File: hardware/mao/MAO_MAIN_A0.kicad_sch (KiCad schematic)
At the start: 0 parts

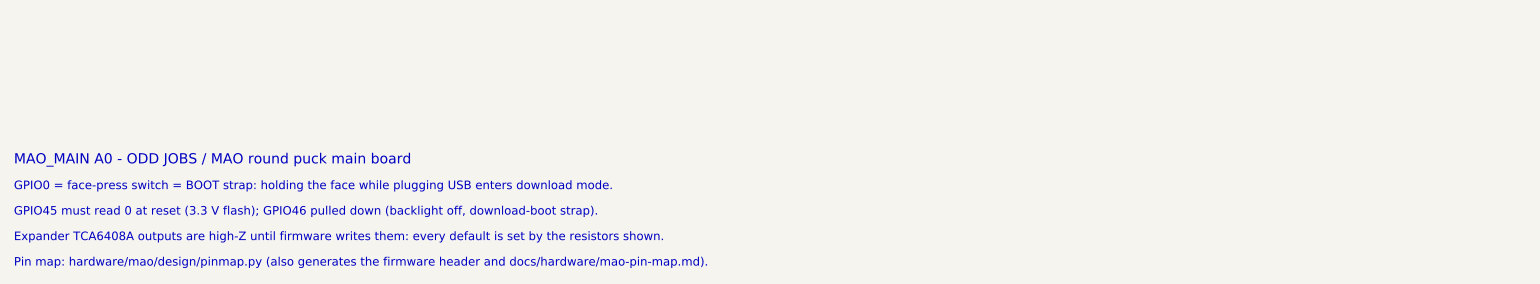
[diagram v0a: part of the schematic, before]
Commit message: hardware: MAO_MAIN A0 4-layer release, plug-in display, ODD JOBS review
- 4 layers (JLC04161H-1080): L1 parts + critical lines, L2 solid GND,
  L3 power regions + slow lines, L4 parts + lines. Re-placed and
  re-routed from scratch: 191 vias (6-layer board: 230).
- J301 HDGC 0.5K-HX-18PWB (C2919497): the round panel plugs in, no
  solder (Winstar 18-pin standard); display TE line added.
- 4-layer pin map; firmware header, pin-map doc and schematic notes
  generated from pinmap.py.
- Pipeline steps: power_regions, plane_check, via_off_pad, snap45 (all
  segments 0/45/90), models3d (datasheet-height bodies for every part).
- Checks: DRC/ERC/parity 0, every L2/L3 plane one piece, silk checker 0,
  Gerbers reviewed independently, firmware 5 configs 0 warnings.
- Mechanical: display standoff 2.7 mm for IR-receiver clearance, ToF
  light-blocking gasket, mic gasket tube, TOP-spring boss; panel tabs at
  2 and 8 o'clock.
- Docs: 4-layer design review, 200-rule ODD JOBS compliance, final
  report, layer plots, Gerber sheet, renders.

Co-Authored-By: Claude Opus 5.5 <noreply@anthropic.com>
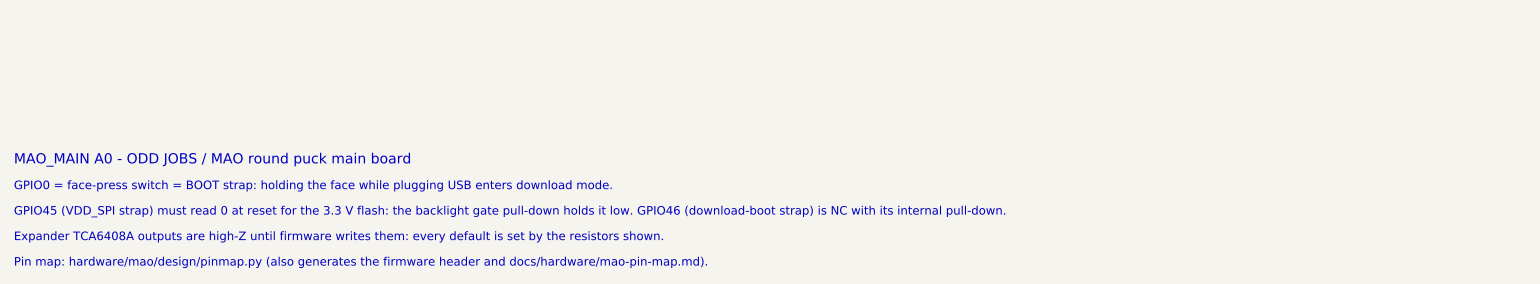
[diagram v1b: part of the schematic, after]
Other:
- note added: "GPIO45 (VDD_SPI strap) must read 0 at reset for the 3.3 V flash: the backlight gate pull-down holds it low. GPIO46 (download-boot strap) is NC with its internal pull-down."
- note removed: "GPIO45 must read 0 at reset (3.3 V flash); GPIO46 pulled down (backlight off, download-boot strap)."
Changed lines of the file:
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@@
 		)
 	)
-	(text "GPIO45 must read 0 at reset (3.3 V flash); GPIO46 pulled down (backlight off, download-boot strap)."
+	(text "GPIO45 (VDD_SPI strap) must read 0 at reset for the 3.3 V flash: the backlight gate pull-down holds it low. GPIO46 (download-boot strap) is NC with its internal pull-down."
 		(exclude_from_sim no)
 		(at 25.4 223.52 0)

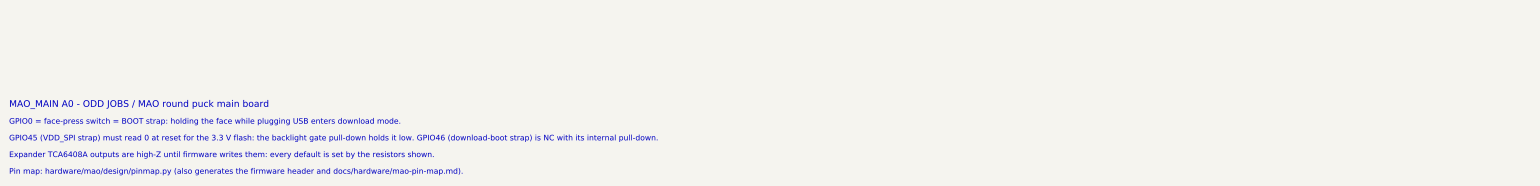
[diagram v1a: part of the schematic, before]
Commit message: MAO A0 revision: stock Winstar panel through a tail slot, AW9364 backlight, routed 4-layer board
Hardware changes from the verification audits:
- display: stock Winstar WF0128BTYAA4DNN0 (70 mm tail) through a routed slot at 9 o'clock
  to J301 on B.Cu; panel pin k on pad 19-k
- backlight: VLED+ on VSYS into an AW9364 (U303) constant-current sink, 40 mA nominal;
  Q301/R303-R305 removed
- display rail: TPS22919 (SC70-6, 1.1 mm: fits under the panel) with its VIN cap; CT cap gone
- +3V3 at 3.18 V (FB 536k), UVLO filter cap, charger ISET 4.3k (207 mA), /CE from the
  expander with a pull-down, charger moved to F under the panel, SD_MODE series 2.2k
- IR_TX on GPIO38, EXP_RST_N on GPIO39 (MTCK reset pull-up lit the IR LEDs)
- IR receiver and ToF pulled inside the ring lip; M2 boss / screw-head keep-outs

Layout: re-placed and re-routed. DRC 0 violations, 0 unconnected; every plane one piece
(the grid router now undoes any L3 route or via that splits a plane); 192 through vias.
Silk: type scale, 6 x 6 S/N field with the JLC order-number placeholder, 4.6 mm back mark,
references kept off vias, and a few easter eggs (a sleeping cat under the face, boop,
meow, 9 lives, MADE FOR BAD IDEAS).

Checks: ERC 0, silk text 0 findings, enclosure check 0 findings (mech_check.py), all
simulations pass (S3 AW9364, S10 TPS22919, S13 207 mA). Docs: bring-up, factory test,
power budget, architecture, mechanical (tail path), pin map. Firmware: dev command
"mao power charge off|on", self-test pad floor for the 3.18 V rail; merge patch regenerated.

Co-Authored-By: Claude Opus 5.5 <noreply@anthropic.com>
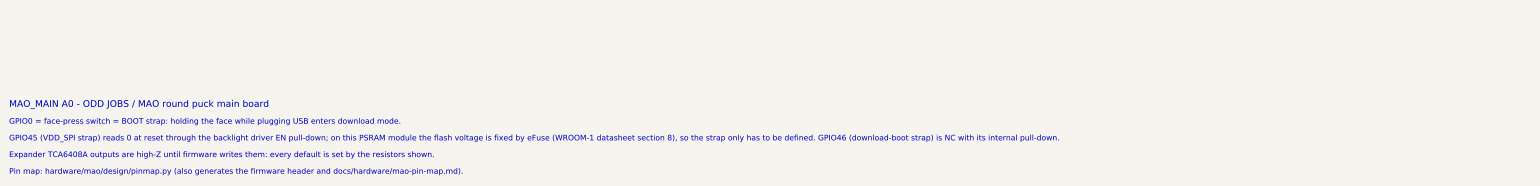
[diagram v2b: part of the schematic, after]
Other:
- note added: "GPIO45 (VDD_SPI strap) reads 0 at reset through the backlight driver EN pull-down; on this PSRAM module the flash voltage is fixed by eFuse (WROOM-1 datasheet section 8), so the strap only has to be defined. GPIO46 (download-boot strap) is NC with its internal pull-down."
- note removed: "GPIO45 (VDD_SPI strap) must read 0 at reset for the 3.3 V flash: the backlight gate pull-down holds it low. GPIO46 (download-boot strap) is NC with its internal pull-down."
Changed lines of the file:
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@@
 		)
 	)
-	(text "GPIO45 (VDD_SPI strap) must read 0 at reset for the 3.3 V flash: the backlight gate pull-down holds it low. GPIO46 (download-boot strap) is NC with its internal pull-down."
+	(text "GPIO45 (VDD_SPI strap) reads 0 at reset through the backlight driver EN pull-down; on this PSRAM module the flash voltage is fixed by eFuse (WROOM-1 datasheet section 8), so the strap only has to be defined. GPIO46 (download-boot strap) is NC with its internal pull-down."
 		(exclude_from_sim no)
 		(at 25.4 223.52 0)

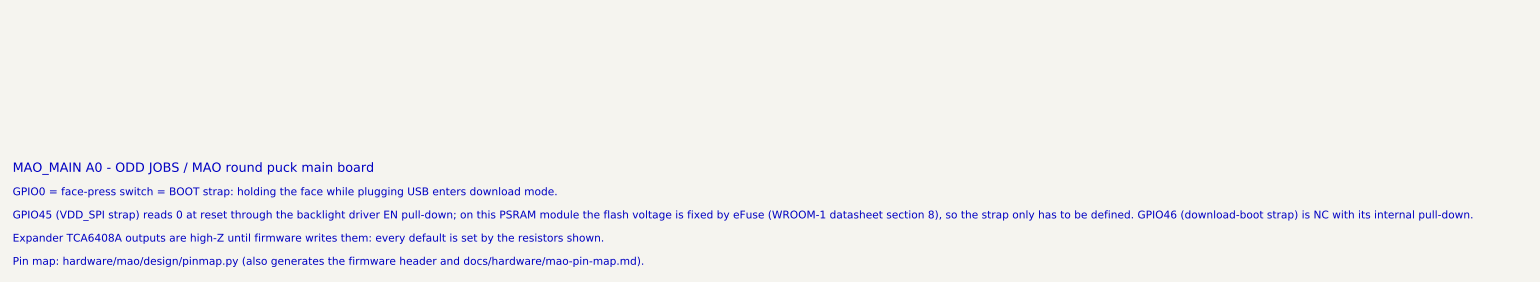
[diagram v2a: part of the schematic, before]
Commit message: MAO A0 final pass: rebuilt board, panel clock option, doc numbers from the final board
Board (rebuilt from design/, DRC 0 / 0 unconnected / parity 0, planes one piece, silk 0, mech 0):
- silk leaders at least one text height (0.8 mm) long; shorter ones read as dashes
- VSYS via at R502 on the pad's axis: every segment at 0/45/90 degrees
- FAB-NOTES notch size generated from mechanical.py (24.0 mm wide, 7.55 mm deep)
- antenna keep-out comments describe what the rule area really covers

Firmware:
- Kconfig MAO_A0_LCD_PCLK_MHZ (10-80, default 80) for the panel SPI clock through the 70 mm tail
- pin map: BOARD_ID routing note; header regenerated
- all five configurations build with 0 warnings; host tests 240 checks pass

Docs: power budget (EN1 strap 11 uA, deep sleep ~85 uA), mechanical (module datum, notch, wall test,
tabs, tail loop and well, LRA), architecture section 6, factory-test pad positions, firmware merge guide
(clock option, reconfigure note), simulation labels (S3 66 mW at 47 mA, S10 t_ON vs rise, S15 deep sleep),
renders, layer plots, Gerber sheet and assembly previews regenerated.

Co-Authored-By: Claude Opus 5.5 <noreply@anthropic.com>
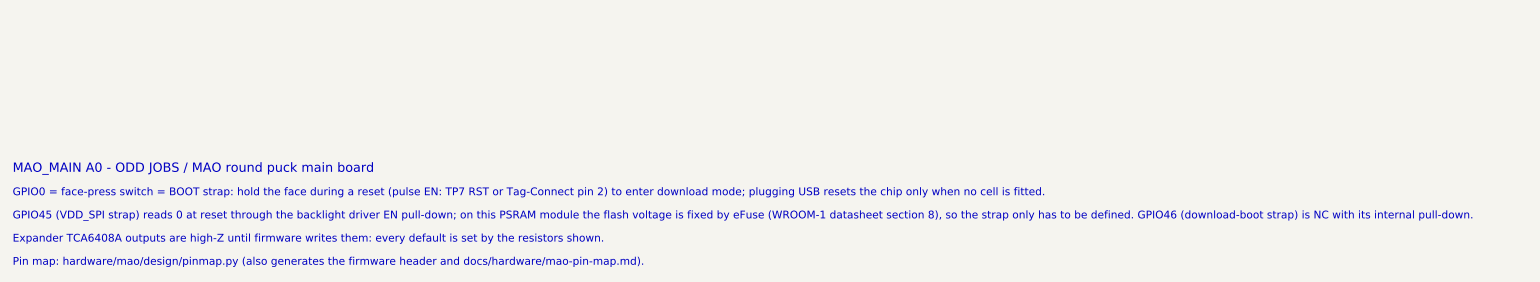
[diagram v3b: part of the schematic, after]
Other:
- note added: "GPIO0 = face-press switch = BOOT strap: hold the face during a reset (pulse EN: TP7 RST or Tag-Connect pin 2) to enter download mode; plugging USB resets the chip only when no cell is fitted."
- note removed: "GPIO0 = face-press switch = BOOT strap: holding the face while plugging USB enters download mode."
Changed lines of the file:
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@@
 		)
 	)
-	(text "GPIO0 = face-press switch = BOOT strap: holding the face while plugging USB enters download mode."
+	(text "GPIO0 = face-press switch = BOOT strap: hold the face during a reset (pulse EN: TP7 RST or Tag-Connect pin 2) to enter download mode; plugging USB resets the chip only when no cell is fitted."
 		(exclude_from_sim no)
 		(at 25.4 219.71 0)
